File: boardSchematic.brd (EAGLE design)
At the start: 100 x 80 mm, 55 parts, among them IC2 TP4056, Q1 BC817-40SMD, Q2 BC817-40SMD, Q3 BC817-40SMD

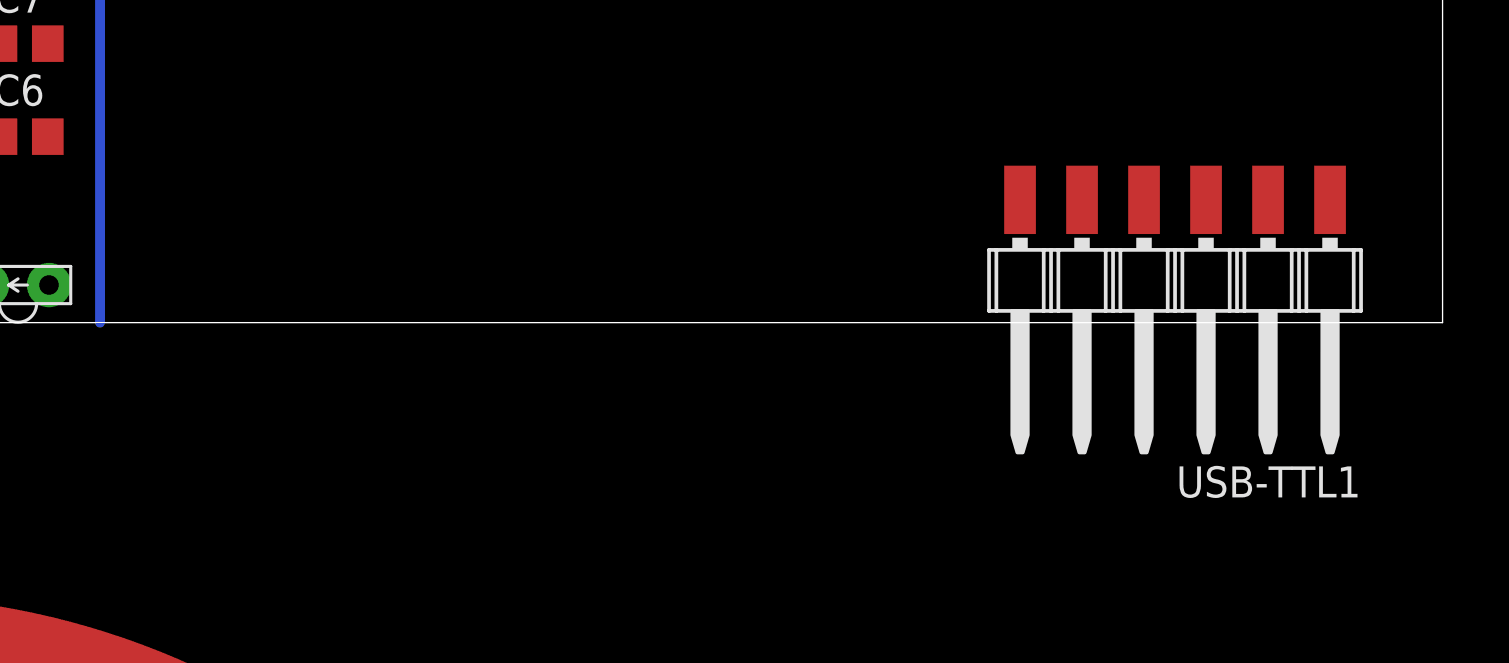
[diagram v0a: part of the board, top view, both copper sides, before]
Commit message: Moved pin header
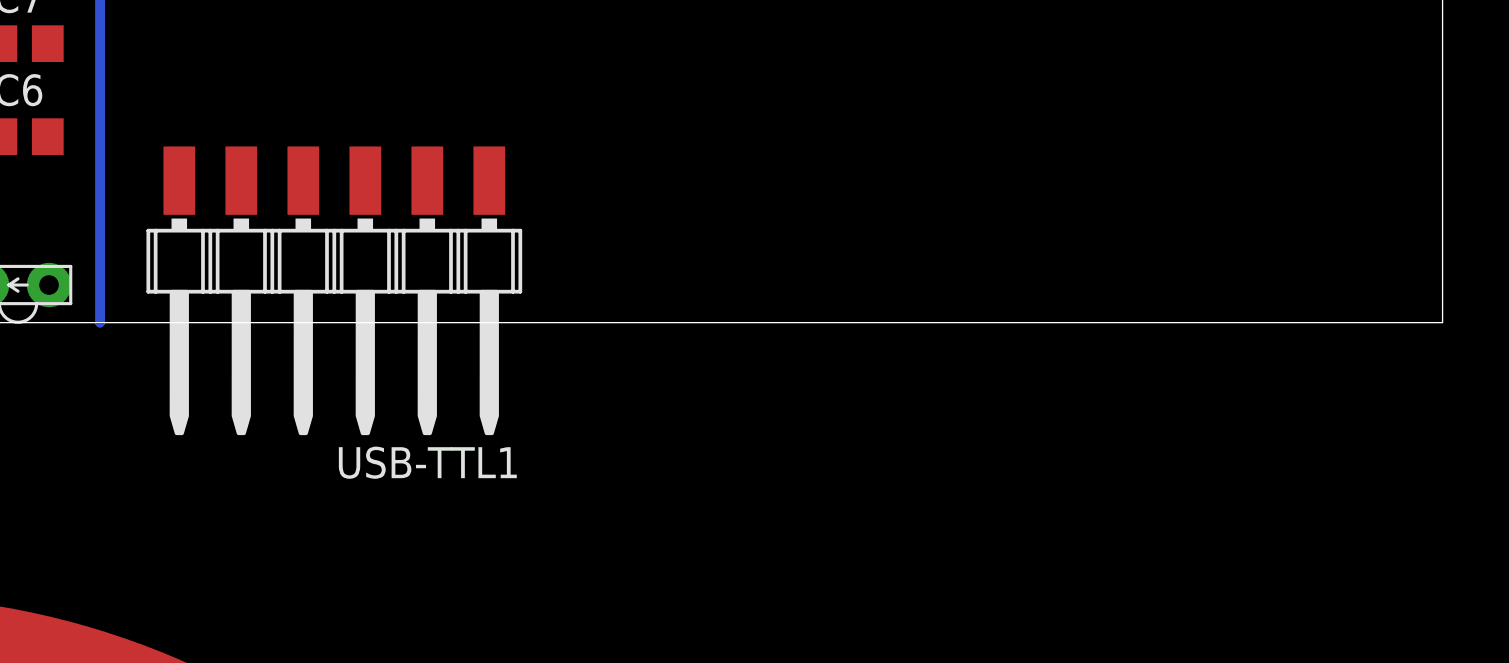
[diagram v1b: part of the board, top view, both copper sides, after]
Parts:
- moved USB-TTL1 34.5 mm to (54.6, 2.52)
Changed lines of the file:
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@@
 <attribute name="PROD_ID" value="VREG-08170" x="61.88" y="33.48" size="1.778" layer="27" display="off"/>
 </element>
-<element name="USB-TTL1" library="dp_devices" package="M1X6_MALE_RIGHT_ANGLED_SMD" value="CON_HEADER_1X06-SMD-RIGHT-ANGLED" x="89.04" y="1.73" rot="R180"/>
+<element name="USB-TTL1" library="dp_devices" package="M1X6_MALE_RIGHT_ANGLED_SMD" value="CON_HEADER_1X06-SMD-RIGHT-ANGLED" x="54.5976" y="2.5174" rot="R180"/>
 <element name="IC2" library="TP4056" package="SOP-8" value="TP4056" x="68.6308" y="68.0212"/>
 <element name="USB1" library="dp_devices" package="CONN_USB_MINI-B" value="CON-USB-F-MINI-B" x="91.9574" y="73.453" rot="R90"/>
@@
 <wire x1="59.5686" y1="30.3812" x2="60.75" y2="25.05" width="0" layer="19" extent="1-1"/>
 <wire x1="76.28" y1="16.35" x2="72.45" y2="26.16" width="0" layer="19" extent="1-1"/>
-<wire x1="82.69" y1="5.03" x2="76.28" y2="16.35" width="0" layer="19" extent="1-1"/>
+<wire x1="48.2476" y1="5.8174" x2="76.28" y2="16.35" width="0" layer="19" extent="1-1"/>
 <wire x1="36.845" y1="15.4638" x2="27.72" y2="33.15" width="0" layer="19" extent="1-1"/>
 <wire x1="42.86" y1="11.43" x2="36.845" y2="15.4638" width="0" layer="19" extent="1-1"/>
@@
 <contactref element="U$1" pad="RXD"/>
 <contactref element="USB-TTL1" pad="3"/>
-<wire x1="90.31" y1="5.03" x2="71.71" y2="38.91" width="0" layer="19" extent="1-1"/>
+<wire x1="55.8676" y1="5.8174" x2="71.71" y2="38.91" width="0" layer="19" extent="1-1"/>
 </signal>
 <signal name="N$5">
@@
 <contactref element="U$1" pad="TXD"/>
 <contactref element="USB-TTL1" pad="2"/>
-<wire x1="92.85" y1="5.03" x2="69.71" y2="38.91" width="0" layer="19" extent="1-1"/>
+<wire x1="58.4076" y1="5.8174" x2="69.71" y2="38.91" width="0" layer="19" extent="1-1"/>
 </signal>
 <signal name="N$27">
 <contactref element="USB-TTL1" pad="4"/>
 <contactref element="R22" pad="1"/>
-<wire x1="64.698" y1="19.62" x2="87.77" y2="5.03" width="0" layer="19" extent="1-1"/>
+<wire x1="64.698" y1="19.62" x2="53.3276" y2="5.8174" width="0" layer="19" extent="1-1"/>
 </signal>
 <signal name="N$3">
